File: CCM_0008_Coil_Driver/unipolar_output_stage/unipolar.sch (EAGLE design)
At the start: 209 parts, among them IC1 AD8675, IC10 AD8675, IC11 AD825, IC12 AD825, IC13 AD825, IC14 AD825, IC15 AD825, IC16 AD825, IC17 BUF634U, IC2 AD797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

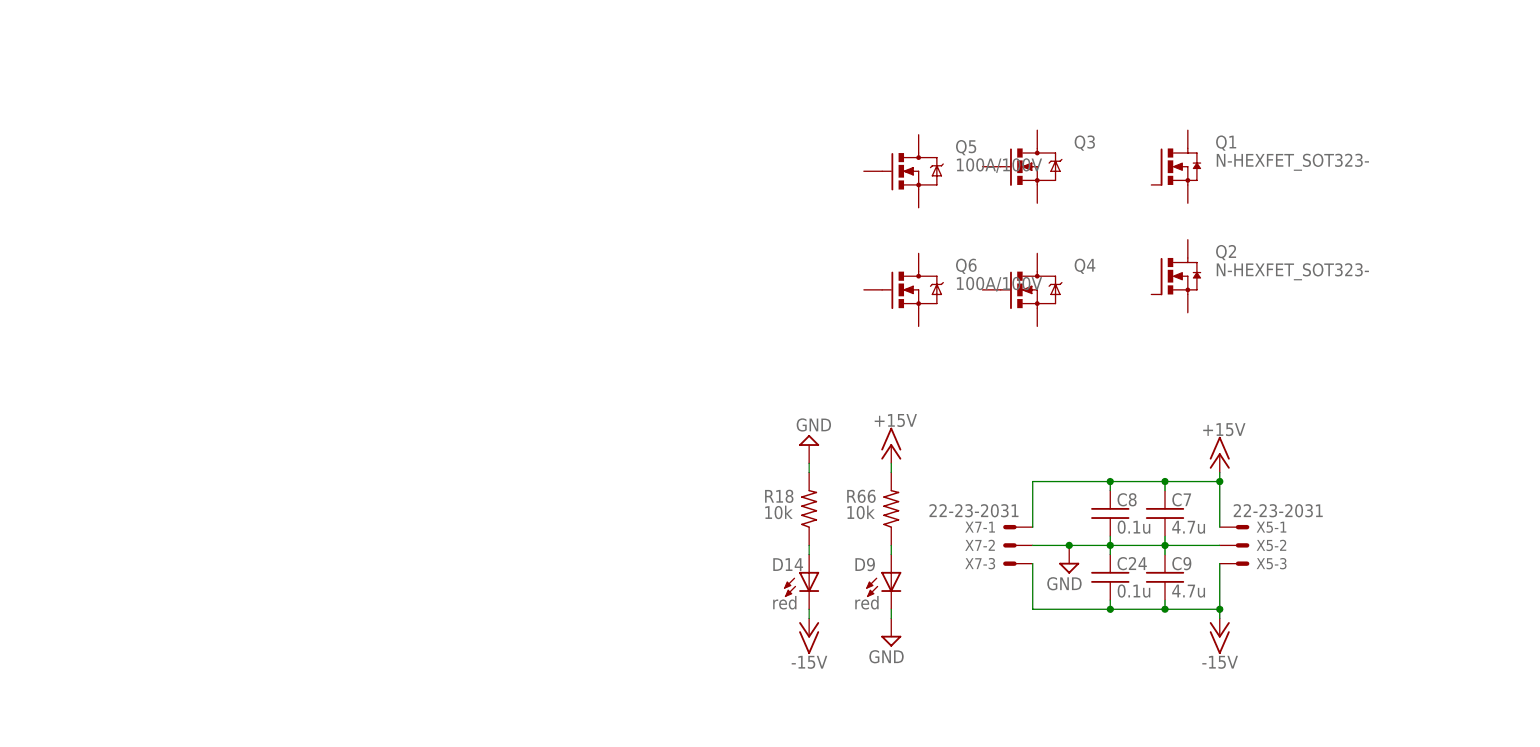
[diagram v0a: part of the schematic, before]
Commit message: CCM_0008: added preliminary output stage design
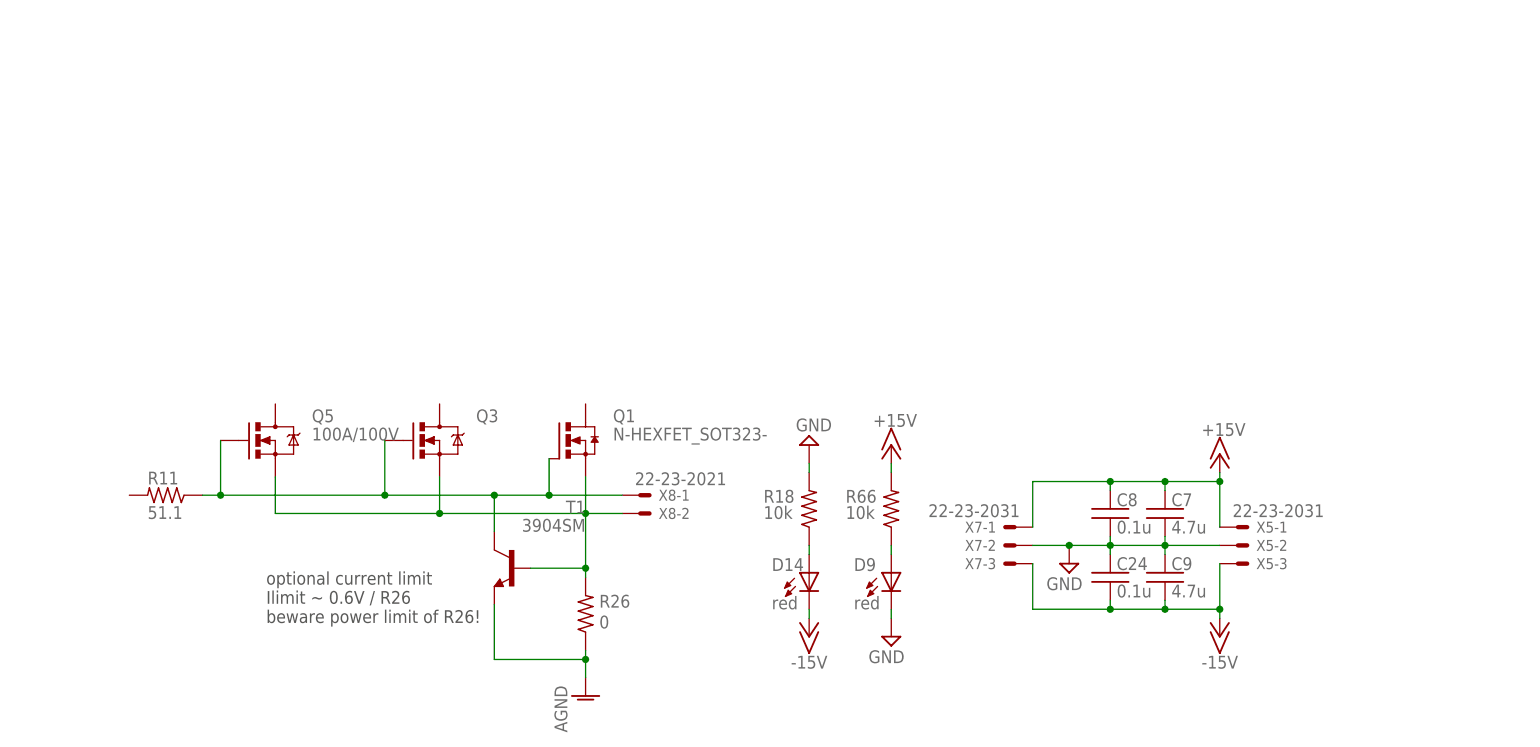
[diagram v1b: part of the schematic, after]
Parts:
- removed Q2: N-HEXFET_SOT323-, transistor-power:N-HEXFET_SOT323-
- removed Q4: (no value), WCSMain:MOSFET-NCHANNELFDD8780
- removed Q6: 100A/100V, WCSMain:MOSFET-NCHANNELPSMN7R0
- added R11: 51.1, acrooptics:R0603
- added R26: 0, noah:RESISTOR2512
- added T1: 3904SM, noah:3904SM
- added X8: 22-23-2021, con-molex:22-23-2021
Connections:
- new net AGND: R26.1, T1.E
- new net N$10: Q1.S, Q3.S, Q5.S, R26.2, T1.B, X8-2.S
- new net N$6: Q1.G, Q3.G, Q5.G, R11.1, T1.C, X8-1.S
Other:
- note added: "optional current limit Ilimit ~ 0.6V / R26 beware power limit of R26!"
- moved on the sheet: Q1, Q3, Q5
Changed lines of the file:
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@@
 <?xml version="1.0" encoding="utf-8"?>
 <!DOCTYPE eagle SYSTEM "eagle.dtd">
-<eagle version="6.5.0">
+<eagle version="8.2.2">
 <drawing>
 <settings>
@@
 <setting verticaltext="up"/>
 </settings>
-<grid distance="0.025" unitdist="inch" unit="inch" style="lines" multiple="1" display="no" altdistance="0.01" altunitdist="inch" altunit="inch"/>
+<grid distance="0.025" unitdist="inch" unit="inch" style="lines" multiple="4" display="yes" altdistance="0.01" altunitdist="inch" altunit="inch"/>
 <layers>
 <layer number="1" name="Top" color="4" fill="1" visible="no" active="no"/>
@@
 <part name="R8" library="acrooptics" deviceset="R" device="0603" value="2.000k"/>
 <part name="Q1" library="transistor-power" deviceset="N-HEXFET_?-*" device="SOT323"/>
-<part name="Q2" library="transistor-power" deviceset="N-HEXFET_?-*" device="SOT323"/>
 <part name="Q3" library="WCSMain" deviceset="MOSFET-NCHANNEL" device="FDD8780"/>
-<part name="Q4" library="WCSMain" deviceset="MOSFET-NCHANNEL" device="FDD8780"/>
 <part name="Q5" library="WCSMain" deviceset="MOSFET-NCHANNEL" device="PSMN7R0" value="100A/100V"/>
-<part name="Q6" library="WCSMain" deviceset="MOSFET-NCHANNEL" device="PSMN7R0" value="100A/100V"/>
+<part name="R11" library="acrooptics" deviceset="R" device="0603" value="51.1"/>
+<part name="X8" library="con-molex" library_urn="urn:adsk.eagle:library:165" deviceset="22-23-2021" device=""/>
+<part name="T1" library="noah" deviceset="3904" device="SM"/>
+<part name="R26" library="noah" deviceset="RESISTOR" device="2512" value="0"/>
+<part name="AGND1" library="supply1" library_urn="urn:adsk.eagle:library:371" deviceset="AGND" device=""/>
 </parts>
 <sheets>
@@
 <text x="322.58" y="228.6" size="1.778" layer="97">+Vbias</text>
 <text x="322.58" y="196.85" size="1.778" layer="97">-Vbias</text>
+<text x="59.69" y="-127" size="1.778" layer="97">optional current limit
+Ilimit ~ 0.6V / R26
+beware power limit of R26!</text>
 </plain>
 <instances>
@@
 <attribute name="VALUE" x="385.445" y="149.733" size="1.778" layer="96"/>
 </instance>
-<instance part="Q1" gate="G$1" x="185.42" y="-63.5"/>
-<instance part="Q2" gate="G$1" x="185.42" y="-78.74"/>
-<instance part="Q3" gate="G$1" x="167.005" y="-63.5"/>
-<instance part="Q4" gate="G$1" x="167.005" y="-80.645"/>
-<instance part="Q5" gate="G$1" x="150.495" y="-64.135"/>
-<instance part="Q6" gate="G$1" x="150.495" y="-80.645"/>
+<instance part="Q1" gate="G$1" x="101.6" y="-101.6"/>
+<instance part="Q3" gate="G$1" x="83.82" y="-101.6"/>
+<instance part="Q5" gate="G$1" x="60.96" y="-101.6"/>
+<instance part="R11" gate="R$1" x="45.72" y="-109.22" smashed="yes" rot="R180">
+<attribute name="NAME" x="43.18" y="-107.7214" size="1.778" layer="95"/>
+<attribute name="VALUE" x="43.18" y="-112.522" size="1.778" layer="96"/>
+</instance>
+<instance part="X8" gate="-1" x="111.76" y="-109.22"/>
+<instance part="X8" gate="-2" x="111.76" y="-111.76"/>
+<instance part="T1" gate="G1" x="93.98" y="-119.38" rot="MR0"/>
+<instance part="R26" gate="G$1" x="104.14" y="-125.73" smashed="yes" rot="R90">
+<attribute name="NAME" x="106.045" y="-124.8664" size="1.778" layer="95"/>
+<attribute name="VALUE" x="106.045" y="-127.762" size="1.778" layer="96"/>
+</instance>
+<instance part="AGND1" gate="VR1" x="104.14" y="-137.16"/>
 </instances>
 <busses>
@@
 </segment>
 </net>
+<net name="N$6" class="0">
+<segment>
+<pinref part="Q5" gate="G$1" pin="G"/>
+<wire x1="53.34" y1="-101.6" x2="53.34" y2="-109.22" width="0.1524" layer="91"/>
+<pinref part="Q3" gate="G$1" pin="G"/>
+<wire x1="53.34" y1="-109.22" x2="76.2" y2="-109.22" width="0.1524" layer="91"/>
+<wire x1="76.2" y1="-109.22" x2="76.2" y2="-101.6" width="0.1524" layer="91"/>
+<pinref part="Q1" gate="G$1" pin="G"/>
+<wire x1="76.2" y1="-109.22" x2="91.44" y2="-109.22" width="0.1524" layer="91"/>
+<wire x1="91.44" y1="-109.22" x2="99.06" y2="-109.22" width="0.1524" layer="91"/>
+<wire x1="99.06" y1="-109.22" x2="99.06" y2="-104.14" width="0.1524" layer="91"/>
+<junction x="76.2" y="-109.22"/>
+<pinref part="R11" gate="R$1" pin="1"/>
+<wire x1="53.34" y1="-109.22" x2="50.8" y2="-109.22" width="0.1524" layer="91"/>
+<junction x="53.34" y="-109.22"/>
+<pinref part="X8" gate="-1" pin="S"/>
+<wire x1="109.22" y1="-109.22" x2="99.06" y2="-109.22" width="0.1524" layer="91"/>
+<junction x="99.06" y="-109.22"/>
+<pinref part="T1" gate="G1" pin="C"/>
+<wire x1="91.44" y1="-114.3" x2="91.44" y2="-109.22" width="0.1524" layer="91"/>
+<junction x="91.44" y="-109.22"/>
+</segment>
+</net>
+<net name="N$10" class="0">
+<segment>
+<pinref part="Q1" gate="G$1" pin="S"/>
+<wire x1="104.14" y1="-106.68" x2="104.14" y2="-111.76" width="0.1524" layer="91"/>
+<pinref part="X8" gate="-2" pin="S"/>
+<wire x1="104.14" y1="-111.76" x2="109.22" y2="-111.76" width="0.1524" layer="91"/>
+<pinref part="Q3" gate="G$1" pin="S"/>
+<wire x1="83.82" y1="-106.68" x2="83.82" y2="-111.76" width="0.1524" layer="91"/>
+<wire x1="83.82" y1="-111.76" x2="104.14" y2="-111.76" width="0.1524" layer="91"/>
+<junction x="104.14" y="-111.76"/>
+<pinref part="Q5" gate="G$1" pin="S"/>
+<wire x1="60.96" y1="-106.68" x2="60.96" y2="-111.76" width="0.1524" layer="91"/>
+<wire x1="60.96" y1="-111.76" x2="83.82" y2="-111.76" width="0.1524" layer="91"/>
+<junction x="83.82" y="-111.76"/>
+<pinref part="T1" gate="G1" pin="B"/>
+<wire x1="104.14" y1="-119.38" x2="96.52" y2="-119.38" width="0.1524" layer="91"/>
+<wire x1="104.14" y1="-111.76" x2="104.14" y2="-119.38" width="0.1524" layer="91"/>
+<pinref part="R26" gate="G$1" pin="2"/>
+<wire x1="104.14" y1="-119.38" x2="104.14" y2="-120.65" width="0.1524" layer="91"/>
+<junction x="104.14" y="-119.38"/>
+</segment>
+</net>
+<net name="AGND" class="0">
+<segment>
+<pinref part="T1" gate="G1" pin="E"/>
+<wire x1="91.44" y1="-132.08" x2="91.44" y2="-124.46" width="0.1524" layer="91"/>
+<pinref part="R26" gate="G$1" pin="1"/>
+<wire x1="91.44" y1="-132.08" x2="104.14" y2="-132.08" width="0.1524" layer="91"/>
+<wire x1="104.14" y1="-132.08" x2="104.14" y2="-130.81" width="0.1524" layer="91"/>
+<pinref part="AGND1" gate="VR1" pin="AGND"/>
+<wire x1="104.14" y1="-134.62" x2="104.14" y2="-132.08" width="0.1524" layer="91"/>
+<junction x="104.14" y="-132.08"/>
+</segment>
+</net>
 </nets>
 </sheet>
@@
 which will not be processed correctly with this version.
 </note>
+<note version="8.2" severity="warning">
+Since Version 8.2, Eagle supports online libraries. The ids
+of those online libraries will not be understood (or retained)
+with this version.
+</note>
 </compatibility>
